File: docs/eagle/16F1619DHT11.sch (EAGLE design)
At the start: 21 parts, among them IC1 74HC595N, IC2 PIC16F1619, J1 DHT11 sensor module, T1 2N2222, T2 2N2222, T3 2N2222, T4 2N2222

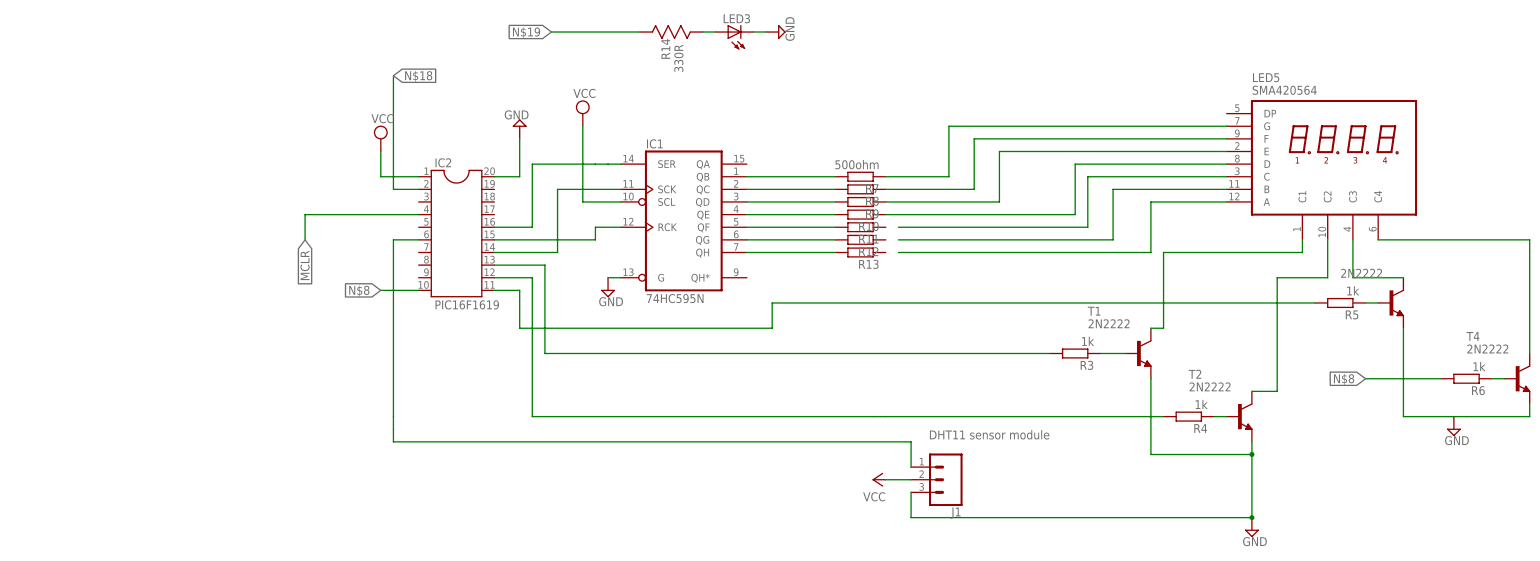
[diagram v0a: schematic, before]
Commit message: change eagle footprint for pic16f1619
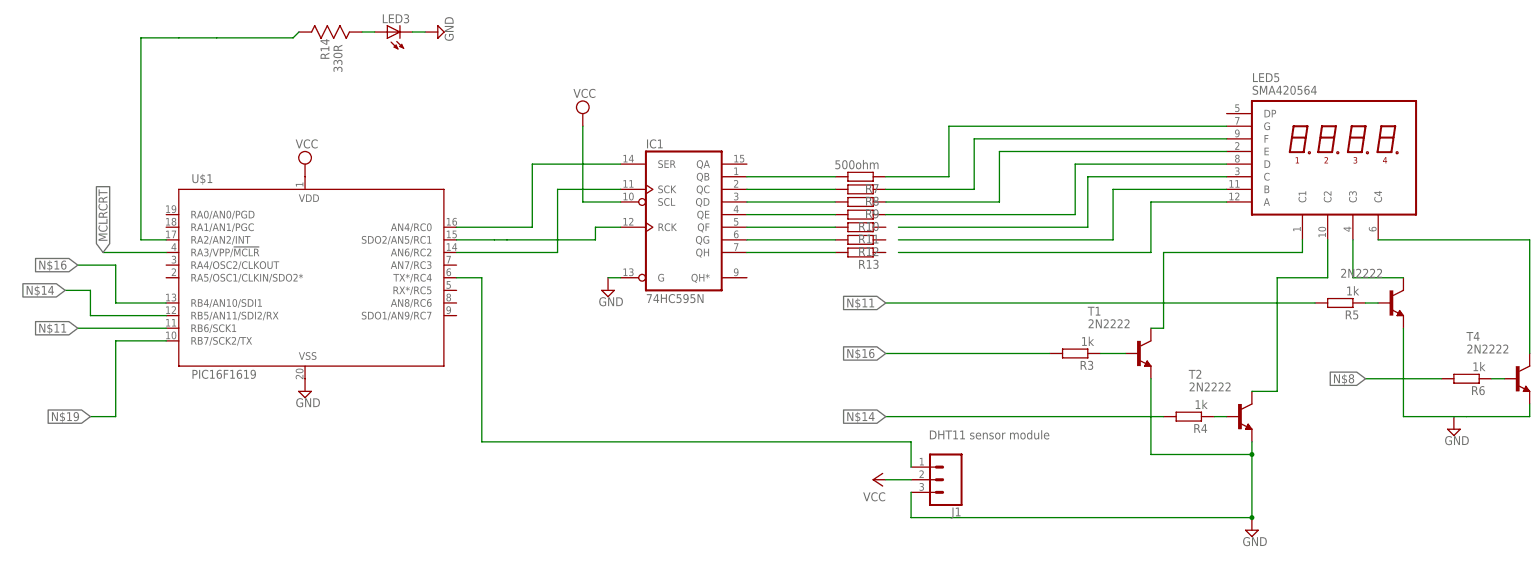
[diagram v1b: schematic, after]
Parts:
- removed IC2: PIC16F1619, ic-package:DIL20
- added U$1: PIC16F1619, SparkFun-IC-Microcontroller:PIC16F1829
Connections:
- removed net MCLR: IC2.4
- removed net N$34: IC2.6, J1.1
- new net MCLRCRT: U$1.RA3/VPP/!MCLR
- net GND: now also U$1.VSS; no longer IC2.20
- net N$1: now also J1.1, U$1.TX*/RC4; no longer IC2.10
- net N$11: now also U$1.RB6/SCK1; no longer IC2.11
- net N$14: now also U$1.RB5/AN11/SDI2/RX; no longer IC2.12
- net N$16: now also U$1.RB4/AN10/SDI1; no longer IC2.13
- net N$18: now also R14.R1, U$1.RA2/AN2/INT; no longer IC2.2
- net N$19: now also U$1.RB7/SCK2/TX; no longer R14.R1
- net N$3: now also U$1.AN6/RC2; no longer IC2.14
- net N$4: now also U$1.SDO2/AN5/RC1; no longer IC2.15
- net N$7: now also U$1.AN4/RC0; no longer IC2.16
- net VCC: now also U$1.VDD; no longer IC2.1
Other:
- moved on the sheet: LED3, R14

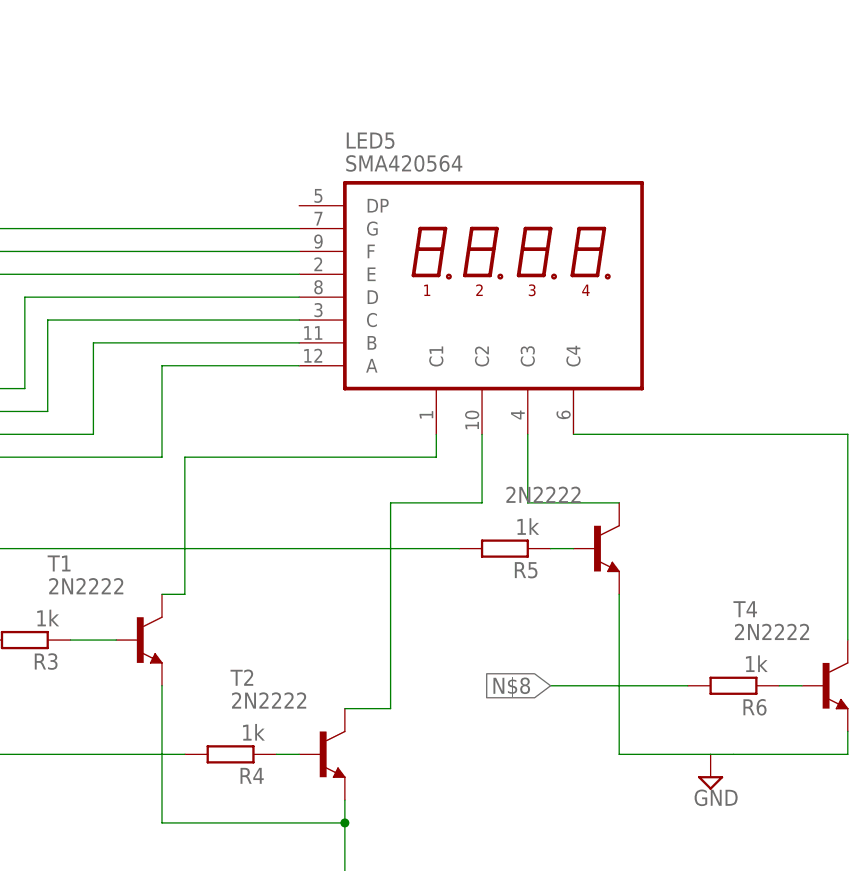
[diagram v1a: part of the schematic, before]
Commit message: adding  new  eagle library footprint to schematic for SMA420564
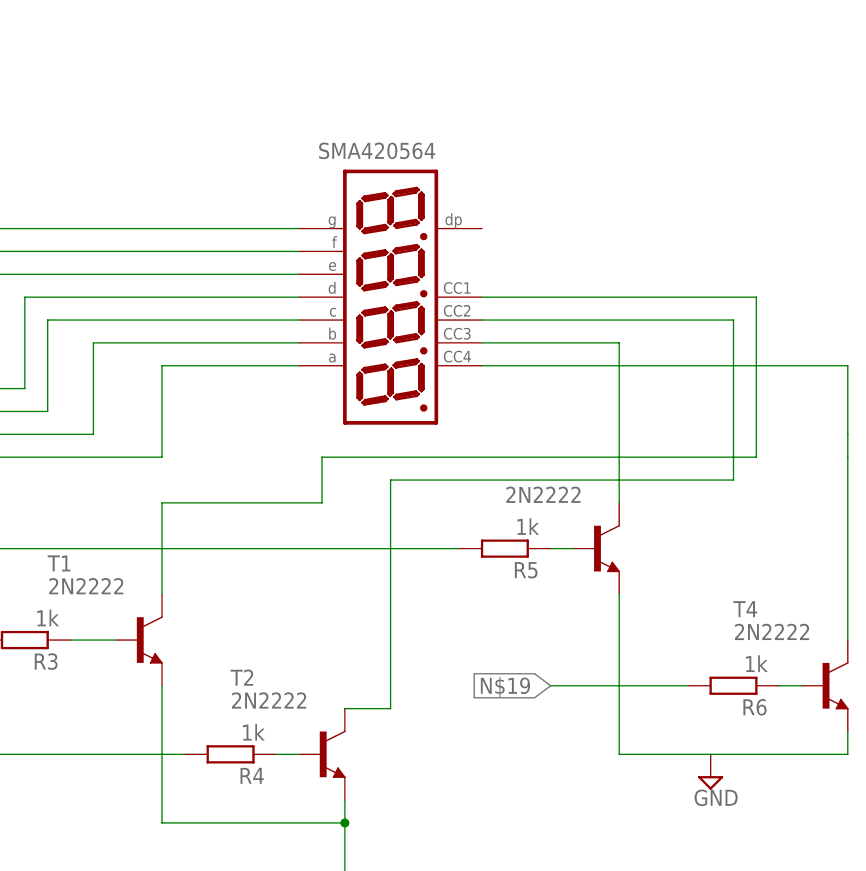
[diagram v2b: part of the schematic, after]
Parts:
- removed LED5: SMA420564, hp-displays:5082-7414
- added SMA420564: NFD-5641AS, display-nfd:NFD-5641AS
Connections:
- removed net N$8: R6.2
- net N$10: now also SMA420564.P$5; no longer LED5.G
- net N$19: now also R6.2
- net N$2: now also SMA420564.P$9; no longer LED5.C2
- net N$24: now also SMA420564.P$8; no longer LED5.C3
- net N$25: now also SMA420564.P$6; no longer LED5.C4
- net N$26: now also SMA420564.P$11; no longer LED5.A
- net N$27: now also SMA420564.P$7; no longer LED5.B
- net N$28: now also SMA420564.P$1; no longer LED5.E
- net N$29: now also SMA420564.P$4; no longer LED5.C
- net N$30: now also SMA420564.P$2; no longer LED5.D
- net N$5: now also SMA420564.P$12; no longer LED5.C1
- net N$9: now also SMA420564.P$10; no longer LED5.F
